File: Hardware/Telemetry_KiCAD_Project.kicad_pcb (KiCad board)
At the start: 4 copper layers, 80 x 93.3 mm, 68 parts, among them J1 TX SPI Debug, J2 RX SPI Debug, J3 50Ω SMA Connector, J4 10118192-0001LF, J5 DB37_Male_MountingHoles, U1 STM32L562VET, U2 Si4463, U3 Si4463, U4 ADL5521, U5 RSD-897.500-942.500-1612-TR, U6 LM317T, U7 USBLC6-2SC6, Y1 32MHz, Y2 32MHz, Y3 32MHz

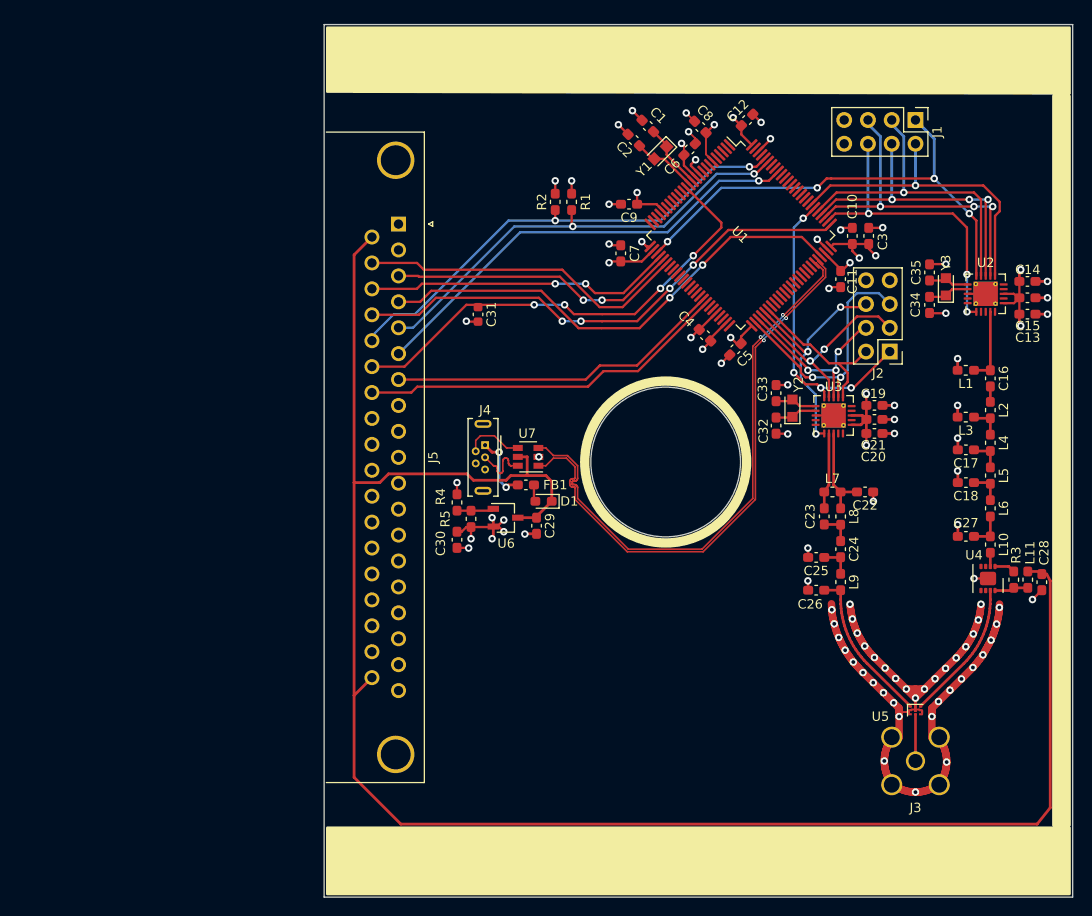
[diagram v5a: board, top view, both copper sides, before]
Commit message: Added copper pours, removed filled zones around RF section
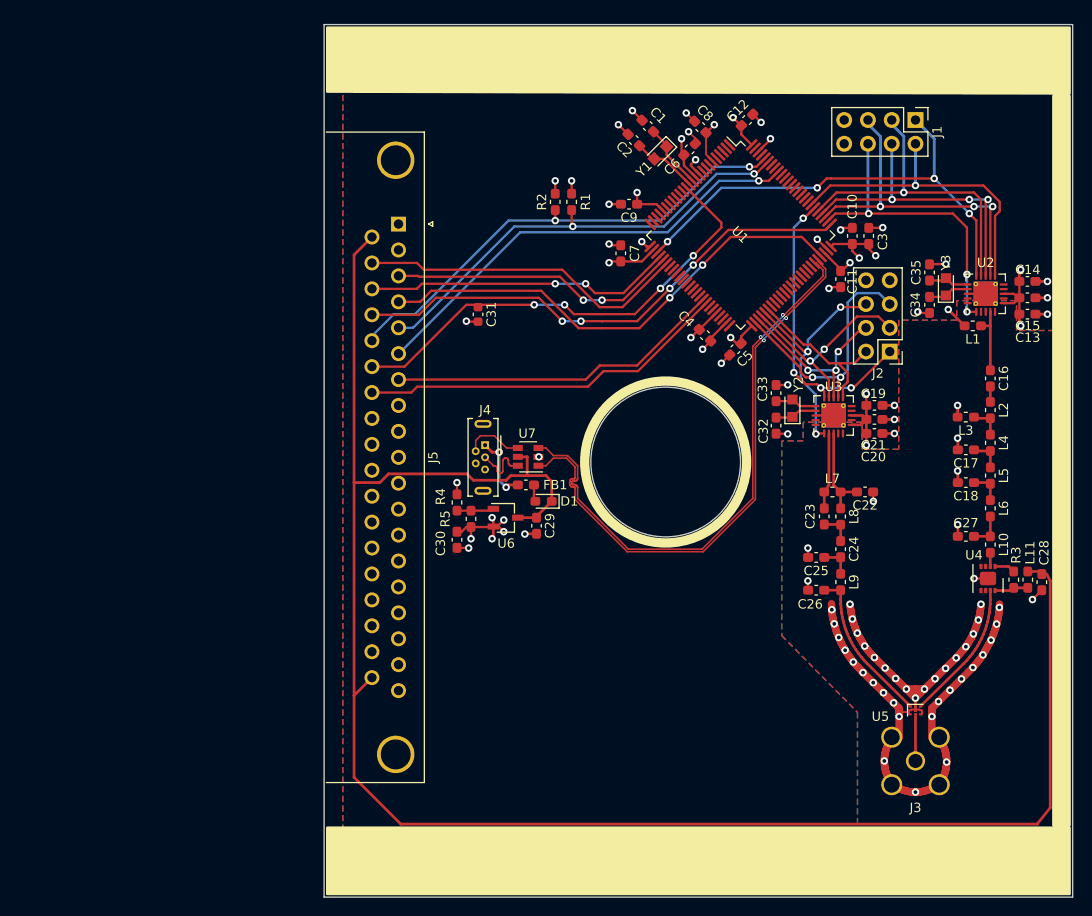
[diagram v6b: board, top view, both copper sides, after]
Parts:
- moved L1 4.81 mm to (176.1, 84.5)
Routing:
- net +3V3: track 74.7 -> 76.1 mm
- net Net-(C16-Pad1): track 7.88 -> 7.25 mm
- added copper zone on B.Cu, net GND
- added copper zone on F.Cu, net GND
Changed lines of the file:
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@@
   (general
     (thickness 1.6)
-    (drawings 241)
+    (drawings 240)
     (tracks 1051)
     (zones 0)
@@
     (2 Pwr.Cu power)
     (31 B.Cu signal)
-    (33 F.Adhes user)
-    (35 F.Paste user)
-    (37 F.SilkS user)
-    (39 F.Mask user)
-    (40 Dwgs.User user)
-    (41 Cmts.User user)
-    (42 Eco1.User user)
-    (43 Eco2.User user)
-    (44 Edge.Cuts user)
-    (45 Margin user)
-    (46 B.CrtYd user)
-    (47 F.CrtYd user)
-    (49 F.Fab user)
+    (33 F.Adhes user hide)
+    (35 F.Paste user hide)
+    (37 F.SilkS user hide)
+    (39 F.Mask user hide)
+    (40 Dwgs.User user hide)
+    (41 Cmts.User user hide)
+    (42 Eco1.User user hide)
+    (43 Eco2.User user hide)
+    (44 Edge.Cuts user hide)
+    (45 Margin user hide)
+    (46 B.CrtYd user hide)
+    (47 F.CrtYd user hide)
+    (49 F.Fab user hide)
   )
   (setup
@@
   )
   (module Inductor_SMD:L_0603_1608Metric_Pad1.05x0.95mm_HandSolder (layer F.Cu)
-    (at 175.375 89.25 180)
+    (at 176.125 84.5 180)
     (descr "Inductor SMD 0603 (1608 Metric), square (rectangular) end terminal, IPC_7351 nominal with elongated pad for handsoldering. (Body size source: http://www.tortai-tech.com/upload/download/2011102023233369053.pdf), generated with kicad-footprint-generator")
     (tags "inductor handsolder")
@@
   (gr_line (start 161.999999 112.75) (end 162 112.749999) (layer F.Mask) (width 0.69337))
   (gr_circle (center 143.3 99.05) (end 151.95 99.05) (layer F.SilkS) (width 1))
-  (gr_circle (center 143.3 99.05) (end 151.75 99.05) (layer Gnd.Cu) (width 1))
   (dimension 17.9 (width 0.15) (layer Dwgs.User)
     (gr_text "17.900 mm" (at 235.7 81.35 90) (layer Dwgs.User)
@@
   (segment (start 164.175001 95.075) (end 164.75 94.500001) (width 0.29337) (layer F.Cu) (net 1))
   (segment (start 163.175 95.075) (end 164.175001 95.075) (width 0.29337) (layer F.Cu) (net 1))
-  (via (at 174.5 88) (size 0.8) (drill 0.4) (layers F.Cu B.Cu) (net 1))
-  (segment (start 174.5 89.25) (end 174.5 88) (width 0.29337) (layer F.Cu) (net 1))
   (segment (start 181.100001 78.750001) (end 181.1 78.75) (width 0.29337) (layer F.Cu) (net 1))
   (segment (start 180.850001 81.5) (end 180.85 81.5) (width 0.29337) (layer F.Cu) (net 1))
@@
   (segment (start 180.5 81.075) (end 181.1 81.5) (width 0.25) (layer F.Cu) (net 1))
   (segment (start 179.425001 81.075) (end 180.5 81.075) (width 0.25) (layer F.Cu) (net 1))
-  (segment (start 145 66) (end 145.25 66.25) (width 0.2) (layer F.Cu) (net 1))
   (segment (start 147.60988 66.174852) (end 148.363425 66.928397) (width 0.2) (layer F.Cu) (net 1))
   (segment (start 147.60988 63.85988) (end 147.60988 66.174852) (width 0.2) (layer F.Cu) (net 1))
-  (via (at 145 65) (size 0.8) (drill 0.4) (layers F.Cu B.Cu) (net 1))
-  (segment (start 145.25 65.25) (end 145 65) (width 0.2) (layer F.Cu) (net 1))
-  (segment (start 145.25 66.25) (end 145.25 65.25) (width 0.2) (layer F.Cu) (net 1))
+  (via (at 145 64.5) (size 0.8) (drill 0.4) (layers F.Cu B.Cu) (net 1))
+  (segment (start 145 66) (end 145.25 66.25) (width 0.25) (layer F.Cu) (net 1))
+  (segment (start 145 64.5) (end 145 66) (width 0.25) (layer F.Cu) (net 1))
+  (via (at 173.5 82.75) (size 0.8) (drill 0.4) (layers F.Cu B.Cu) (net 1))
+  (segment (start 175.25 84.5) (end 173.5 82.75) (width 0.29337) (layer F.Cu) (net 1))
   (via (at 167.75 96) (size 0.8) (drill 0.4) (layers F.Cu B.Cu) (net 2))
   (via (at 165.5 103.25) (size 0.8) (drill 0.4) (layers F.Cu B.Cu) (net 2))
@@
   (via (at 184.1 79.75) (size 0.8) (drill 0.4) (layers F.Cu B.Cu) (net 2))
   (via (at 174.5 105.75) (size 0.8) (drill 0.4) (layers F.Cu B.Cu) (net 2))
-  (via (at 173.25 83.15) (size 0.8) (drill 0.4) (layers F.Cu B.Cu) (net 2))
   (via (at 184.1 83.25) (size 0.8) (drill 0.4) (layers F.Cu B.Cu) (net 2))
   (via (at 173.25 77.9) (size 0.8) (drill 0.4) (layers F.Cu B.Cu) (net 2))
@@
   (segment (start 173.225001 77.925) (end 173.25 77.9) (width 0.25) (layer F.Cu) (net 2))
   (segment (start 182.825001 79.75) (end 184.1 79.75) (width 0.29337) (layer F.Cu) (net 2))
-  (segment (start 173.225 83.125) (end 173.25 83.15) (width 0.25) (layer F.Cu) (net 2))
   (segment (start 182.825 81.5) (end 184.1 81.5) (width 0.29337) (layer F.Cu) (net 2))
   (segment (start 182.825001 83.25) (end 184.1 83.25) (width 0.29337) (layer F.Cu) (net 2))
@@
   (via (at 169.999999 134.331193) (size 0.8) (drill 0.4) (layers F.Cu B.Cu) (net 2))
   (segment (start 171.525 83.15) (end 171.5 83.125) (width 0.25) (layer F.Cu) (net 2))
-  (segment (start 173.25 83.15) (end 171.525 83.15) (width 0.25) (layer F.Cu) (net 2))
   (segment (start 171.525 77.9) (end 171.5 77.925) (width 0.25) (layer F.Cu) (net 2))
   (segment (start 173.25 77.9) (end 171.525 77.9) (width 0.25) (layer F.Cu) (net 2))
@@
   (segment (start 170.05 123.51) (end 169.99 124.28) (width 0.2) (layer F.Cu) (net 2))
   (via (at 169.99 124.28) (size 0.8) (drill 0.4) (layers F.Cu B.Cu) (net 2))
+  (via (at 170.25 83) (size 0.8) (drill 0.4) (layers F.Cu B.Cu) (net 2))
+  (segment (start 170.375 83.125) (end 170.25 83) (width 0.25) (layer F.Cu) (net 2))
+  (segment (start 171.5 83.125) (end 170.375 83.125) (width 0.25) (layer F.Cu) (net 2))
   (segment (start 178 106.999999) (end 178 104.874999) (width 0.29337) (layer F.Cu) (net 3))
   (segment (start 178 106.999999) (end 176.25 106.999999) (width 0.29337) (layer F.Cu) (net 3))
@@
   (segment (start 142.095926 66.654074) (end 143.139355 66.654074) (width 0.25) (layer F.Cu) (net 95))
   (segment (start 178 92.624999) (end 178 90.975) (width 0.29337) (layer F.Cu) (net 96))
-  (segment (start 178 89.25) (end 176.374999 89.25) (width 0.29337) (layer F.Cu) (net 97))
   (segment (start 178 83.000001) (end 178.000001 83) (width 0.29337) (layer F.Cu) (net 97))
-  (segment (start 178 89.250001) (end 178 83.000001) (width 0.29337) (layer F.Cu) (net 97))
+  (segment (start 177 84.5) (end 178 84.5) (width 0.29337) (layer F.Cu) (net 97))
+  (segment (start 178 84.5) (end 178 83.000001) (width 0.29337) (layer F.Cu) (net 97))
+  (segment (start 178 89.250001) (end 178 84.5) (width 0.29337) (layer F.Cu) (net 97))
   (segment (start 176.4875 97.875) (end 176.3625 97.75) (width 0.29337) (layer F.Cu) (net 98))
   (segment (start 178 99.625) (end 178 97.875) (width 0.29337) (layer F.Cu) (net 98))
@@
   (segment (start 127.75 74.5) (end 143.5 74.5) (width 0.25) (layer B.Cu) (net 139))
   (segment (start 114.75 87.47) (end 114.78 87.47) (width 0.25) (layer B.Cu) (net 139))
-  (zone (net 2) (net_name GND) (layer Gnd.Cu) (hatch edge 0.508)
-    (connect_pads (clearance 0.508))
-    (min_thickness 0.254)
-    (fill yes (arc_segments 32) (thermal_gap 0.508) (thermal_bridge_width 0.508))
-    (polygon
-      (pts
-        (xy 186.6 142.4) (xy 107 142.2) (xy 107 55.4) (xy 186.6 55.4)
-      )
-    )
-  )
-  (zone (net 1) (net_name +3V3) (layer Pwr.Cu) (hatch edge 0.508)
-    (connect_pads (clearance 0.508))
-    (min_thickness 0.254)
-    (fill yes (arc_segments 32) (thermal_gap 0.508) (thermal_bridge_width 0.508))
-    (polygon
-      (pts
-        (xy 186.6 142.4) (xy 107 142.2) (xy 107 55.4) (xy 186.6 55.4)
-      )
-    )
-  )
   (zone (net 0) (net_name "") (layer F.SilkS) (hatch edge 0.508)
     (connect_pads (clearance 0.508))
@@
       )
     )
+  )
+  (zone (net 2) (net_name GND) (layer Gnd.Cu) (hatch edge 0.508)
+    (connect_pads (clearance 0.508))
+    (min_thickness 0.254)
+    (fill yes (arc_segments 32) (thermal_gap 0.508) (thermal_bridge_width 0.508))
+    (polygon
+      (pts
+        (xy 184.8 140.5) (xy 108.8 140.5) (xy 108.8 57.3) (xy 184.8 57.3)
+      )
+    )
+  )
+  (zone (net 2) (net_name GND) (layer Gnd.Cu) (hatch edge 0.508)
+    (connect_pads (clearance 0.508))
+    (min_thickness 0.254)
+    (fill yes (arc_segments 32) (thermal_gap 0.508) (thermal_bridge_width 0.508))
+    (polygon
+      (pts
+        (xy 144.75 65.5) (xy 144 66.25) (xy 147.25 69.5) (xy 146.5 70.25) (xy 143.25 67)
+        (xy 142.25 68) (xy 137.25 63) (xy 138.25 62) (xy 137.75 61.5) (xy 138.25 61)
+        (xy 138.75 61.5) (xy 139.75 60.5)
+      )
+    )
+  )
+  (zone (net 1) (net_name +3V3) (layer Pwr.Cu) (hatch edge 0.508)
+    (connect_pads (clearance 0.508))
+    (min_thickness 0.254)
+    (fill yes (arc_segments 32) (thermal_gap 0.508) (thermal_bridge_width 0.508))
+    (polygon
+      (pts
+        (xy 184.8 85) (xy 180.8 85) (xy 180.8 81.8) (xy 174.4 81.8) (xy 174.4 83.9)
+        (xy 168.2 83.9) (xy 168.2 97.7) (xy 164.3 97.7) (xy 164.3 94.8) (xy 158 94.8)
+        (xy 158 96.8) (xy 155.7 96.8) (xy 155.7 117.6) (xy 157.9 119.8) (xy 163.8 125.8)
+        (xy 163.8 140.5) (xy 108.8 140.5) (xy 108.8 57.3) (xy 184.8 57.3)
+      )
+    )
+  )
+  (zone (net 2) (net_name GND) (layer B.Cu) (hatch edge 0.508)
+    (connect_pads (clearance 0.508))
+    (min_thickness 0.254)
+    (fill yes (arc_segments 32) (thermal_gap 0.508) (thermal_bridge_width 0.508))
+    (polygon
+      (pts
+        (xy 184.8 85) (xy 180.8 85) (xy 180.8 81.8) (xy 174.4 81.8) (xy 174.4 83.9)
+        (xy 168.2 83.9) (xy 168.2 97.7) (xy 164.3 97.7) (xy 164.3 94.8) (xy 158 94.8)
+        (xy 158 96.8) (xy 155.7 96.8) (xy 155.7 117.6) (xy 163.8 125.8) (xy 163.8 140.5)
+        (xy 108.8 140.5) (xy 108.8 57.3) (xy 184.8 57.3)
+      )
+    )
+  )
+  (zone (net 2) (net_name GND) (layer F.Cu) (hatch edge 0.508)
+    (connect_pads (clearance 0.508))
+    (min_thickness 0.254)
+    (fill yes (arc_segments 32) (thermal_gap 0.508) (thermal_bridge_width 0.508))
+    (polygon
+      (pts
+        (xy 184.8 85) (xy 180.8 85) (xy 180.8 81.8) (xy 174.4 81.8) (xy 174.4 83.9)
+        (xy 168.2 83.9) (xy 168.2 97.7) (xy 164.3 97.7) (xy 164.3 94.8) (xy 158 94.8)
+        (xy 158 96.8) (xy 155.7 96.8) (xy 155.7 117.6) (xy 163.8 125.8) (xy 163.8 140.5)
+        (xy 108.8 140.5) (xy 108.8 57.3) (xy 184.8 57.3)
+      )
+    )
